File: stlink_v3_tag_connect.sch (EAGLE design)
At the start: 10 parts, among them CON1 STLINK_V3_HAT_SWD/JTAG_MINIMAL, J1 RJ12, U1 SN74LVC2T45DCU

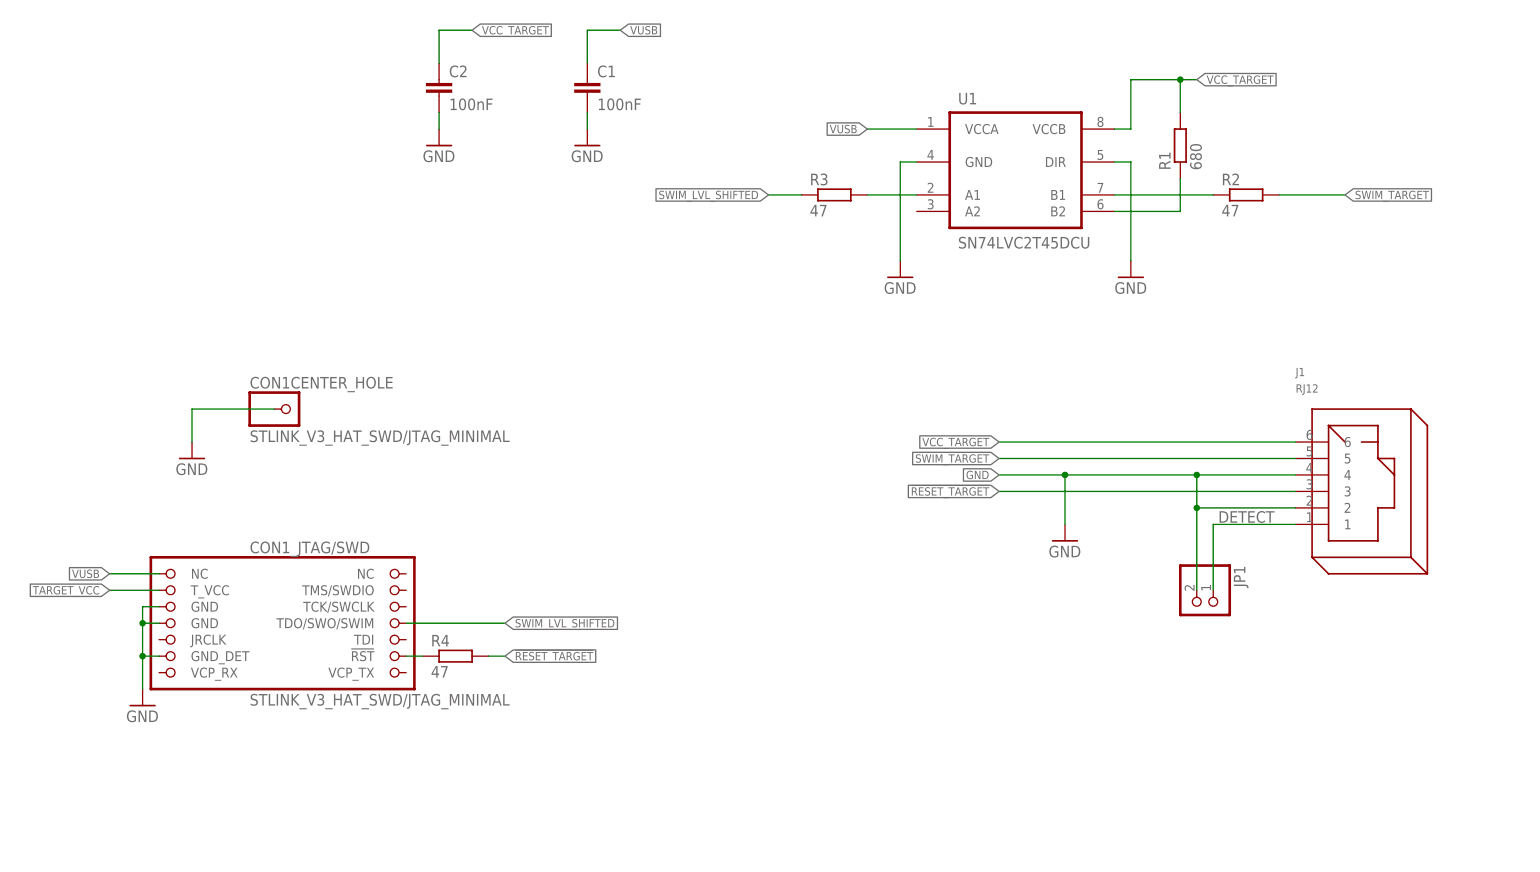
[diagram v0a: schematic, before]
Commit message: Added SWD popoption
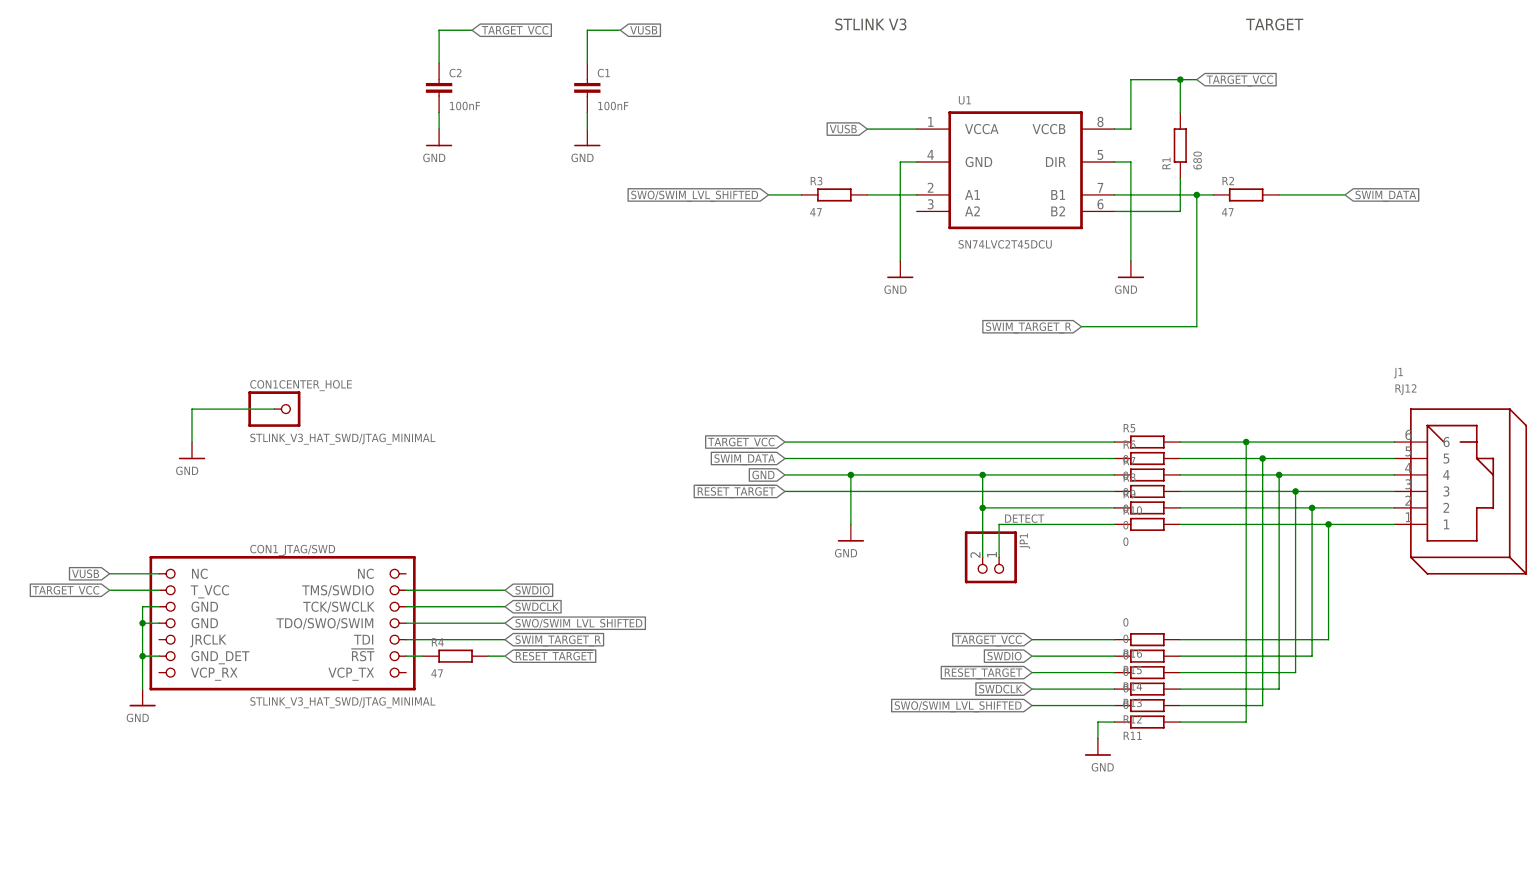
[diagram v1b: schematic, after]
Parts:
- added R10, R11, R12, R13, R14, R15, R16, R5, R6, R7, R8, R9: 0, resistor:R-EU_R0603
- JP1: value (none) -> -
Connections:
- removed net SWIM_LVL_SHIFTED: CON1_JTAG/SWD.TDO/SWO/SWIM, R3.1
- removed net SWIM_TARGET: J1.5, R2.2
- removed net VCC_TARGET: C2.1, J1.6, R1.2, U1.VCCB
- new net N$12: J1.6, R11.2, R5.2
- new net N$3: J1.5, R12.2, R6.2
- new net N$4: J1.4, R13.2, R7.2
- new net N$5: J1.3, R14.2, R8.2
- new net N$6: J1.2, R15.2, R9.2
- new net N$7: J1.1, R10.2, R16.2
- new net SWDCLK: CON1_JTAG/SWD.TCK/SWCLK, R13.1
- new net SWDIO: CON1_JTAG/SWD.TMS/SWDIO, R15.1
- new net SWIM_DATA: R2.2, R6.1
- new net SWO/SWIM_LVL_SHIFTED: CON1_JTAG/SWD.TDO/SWO/SWIM, R12.1, R3.1
- net !RESET_TARGET: now also R14.1, R8.1; no longer J1.3
- net DETECT: now also R10.1; no longer J1.1
- net GND: now also R11.1, R7.1, R9.1; no longer J1.2, J1.4
- net SWIM_TARGET_R: now also CON1_JTAG/SWD.TDI
- net TARGET_VCC: now also C2.1, R1.2, R16.1, R5.1, U1.VCCB
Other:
- note added: "STLINK V3"
- note added: "TARGET"
- moved on the sheet: J1, JP1

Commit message: - Added mgt MCU - Moved RJ12 to the middle - Fixed SWD pinout
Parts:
- removed J1: RJ12, con-rj:RJ12
- added C3: 100nF, rcl:C-EUC0603K
- added C4, C5, C7: 1uF, rcl:C-EUC0603
- added C6: 470pF, rcl:C-EUC0603
- added CON2: TC2030-MCP-SWD, tag-connect:TC2030-MCP-SWD
- added IC1: STM8S003F3, stm8:STM8S003F3
- added LED1, LED2, LED3: Red, SparkFun:LED0603
- added R17: 10K, rcl:R-EU_R0603
- added R18, R19, R20: 1K, rcl:R-EU_R0603
- added SWIM: SWIM_254, swim:SWIM_254
- added U3: MIC5205-3.3YM5-TR, LTC_By_element14_Batch_1:LT1761ES5-3.3TRMPBF
- R11, R16: value 0 -> 10K; device resistor:R-EU_R0603 -> rcl:R-EU_R0603
- R5, R9: value 0 -> 47; device resistor:R-EU_R0603 -> rcl:R-EU_R0603
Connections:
- removed net N$12: J1.6, R11.2, R5.2
- removed net N$6: J1.2, R15.2, R9.2
- removed net N$7: J1.1, R10.2, R16.2
- new net !RESET_TARGET!/SWDCLK: CON2.SWCLK/TCK, R13.2, R8.2
- new net !RST: IC1.!RST, SWIM.!RST
- new net +3V3: C3.1, C5.1, IC1.VDD, R17.1, R19.2, SWIM.VDD, U3.OUT
- new net DETECT/SWO: CON2.SWO/TDO, R10.2, R12.2
- new net DGND: LED1.C, LED2.C, LED3.C
- new net GND/!RESET_TARGET!: CON2.!RESET, R14.2, R7.2
- new net MIC_BYPASS: C6.1, U3.BYP
- new net N$2: CON1_JTAG/SWD.VCP_TX, R5.1
- new net N$38: LED2.A, R18.1
- new net STM8_RX: IC1.PD6/UART1_RX/AIN6, R5.2
- new net STM8_SWIM: IC1.PD1/SWIM, SWIM.DATA
- new net STM8_TX: IC1.PD5/UART1_TX/AIN5, R9.1
- new net SWIM_DATA/SWDIO: CON2.SWDIO/TMS, R15.2, R6.2
- new net TARGET_VCC_DETECT: IC1.PC4/TIM1_CH4/CLK_CCO/AIN2/[!TIM1_CH2!], R11.2, R16.2
- new net VBAT: C4.1, U3.IN, U3.~SHDN
- new net VCAP1: C7.1, IC1.VCAP
- net DETECT: now also IC1.PA3/TIM2_CH3/[SPI_NSS], R17.2
- net GND: now also C3.2, C4.2, C5.2, C6.2, C7.2, CON2.GND, IC1.GND, SWIM.GND, U3.GND; no longer R9.1
- net N$3: now also CON1_JTAG/SWD.VCP_RX, R9.2; no longer J1.5, R12.2, R6.2
- net N$4: now also LED1.A, R19.1; no longer J1.4, R13.2, R7.2
- net N$5: now also LED3.A, R20.1; no longer J1.3, R14.2, R8.2
- net TARGET_VCC: now also CON2.VCC, R18.2; no longer R5.1
- net VUSB: now also R20.2

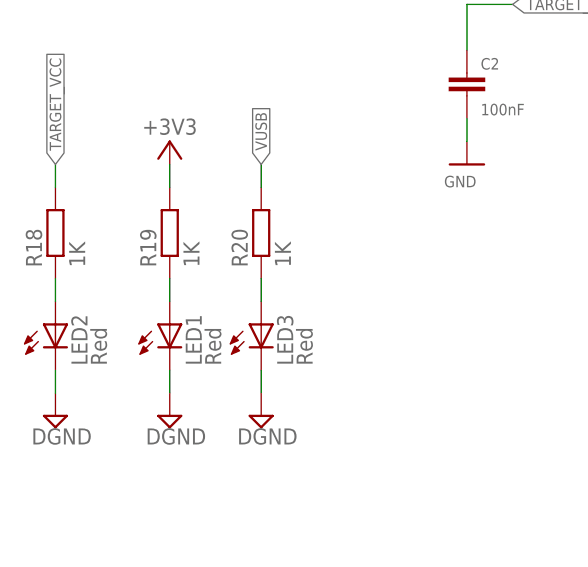
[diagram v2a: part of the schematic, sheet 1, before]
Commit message: Align LEDs
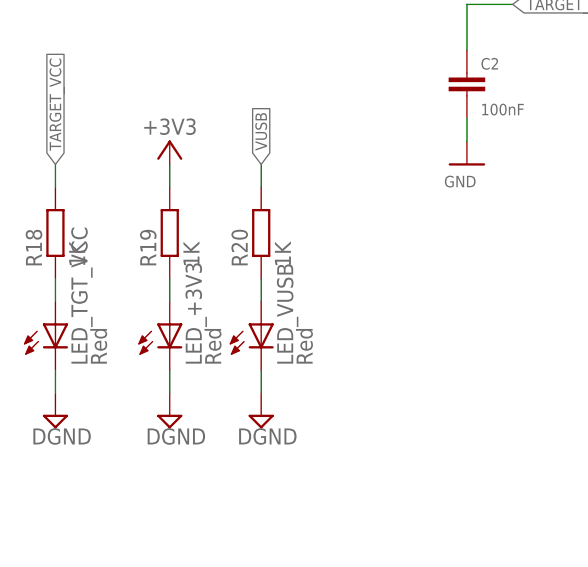
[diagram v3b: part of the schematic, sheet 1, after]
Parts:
- renumbered LED1 to LED_+3V3, LED2 to LED_TGT_VCC, LED3 to LED_VUSB
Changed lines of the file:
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@@
 <attribute name="OC_FARNELL" value="2130354"/>
 </part>
-<part name="LED2" library="SparkFun" deviceset="LED" device="0603" value="Red"/>
+<part name="LED_TGT_VCC" library="SparkFun" deviceset="LED" device="0603" value="Red"/>
 <part name="SUPPLY9" library="supply2" deviceset="DGND" device=""/>
 <part name="R19" library="rcl" deviceset="R-EU_" device="R0603" value="1K">
 <attribute name="OC_FARNELL" value="2130354"/>
 </part>
-<part name="LED1" library="SparkFun" deviceset="LED" device="0603" value="Red"/>
+<part name="LED_+3V3" library="SparkFun" deviceset="LED" device="0603" value="Red"/>
 <part name="SUPPLY1" library="supply2" deviceset="DGND" device=""/>
 <part name="+3V4" library="supply1" deviceset="+3V3" device=""/>
@@
 <attribute name="OC_FARNELL" value="2130354"/>
 </part>
-<part name="LED3" library="SparkFun" deviceset="LED" device="0603" value="Red"/>
+<part name="LED_VUSB" library="SparkFun" deviceset="LED" device="0603" value="Red"/>
 <part name="SUPPLY2" library="supply2" deviceset="DGND" device=""/>
 <part name="FRAME2" library="martonmiklos" deviceset="A4L-LOC" device="" value="PAGE1"/>
@@
 <attribute name="VALUE" x="23.622" y="138.43" size="1.778" layer="96" rot="R90"/>
 </instance>
-<instance part="LED2" gate="G$1" x="20.32" y="132.08" smashed="yes">
+<instance part="LED_TGT_VCC" gate="G$1" x="20.32" y="132.08" smashed="yes">
 <attribute name="NAME" x="23.876" y="127.508" size="1.778" layer="95" rot="R90"/>
 <attribute name="VALUE" x="26.035" y="127.508" size="1.778" layer="96" rot="R90"/>
@@
 <attribute name="VALUE" x="36.322" y="138.43" size="1.778" layer="96" rot="R90"/>
 </instance>
-<instance part="LED1" gate="G$1" x="33.02" y="132.08" smashed="yes">
+<instance part="LED_+3V3" gate="G$1" x="33.02" y="132.08" smashed="yes">
 <attribute name="NAME" x="36.576" y="127.508" size="1.778" layer="95" rot="R90"/>
 <attribute name="VALUE" x="38.735" y="127.508" size="1.778" layer="96" rot="R90"/>
@@
 <attribute name="VALUE" x="46.482" y="138.43" size="1.778" layer="96" rot="R90"/>
 </instance>
-<instance part="LED3" gate="G$1" x="43.18" y="132.08" smashed="yes">
+<instance part="LED_VUSB" gate="G$1" x="43.18" y="132.08" smashed="yes">
 <attribute name="NAME" x="46.736" y="127.508" size="1.778" layer="95" rot="R90"/>
 <attribute name="VALUE" x="48.895" y="127.508" size="1.778" layer="96" rot="R90"/>
@@
 <segment>
 <wire x1="20.32" y1="124.46" x2="20.32" y2="127" width="0.1524" layer="91"/>
-<pinref part="LED2" gate="G$1" pin="C"/>
+<pinref part="LED_TGT_VCC" gate="G$1" pin="C"/>
 <pinref part="SUPPLY9" gate="G$1" pin="DGND"/>
 </segment>
 <segment>
 <wire x1="33.02" y1="124.46" x2="33.02" y2="127" width="0.1524" layer="91"/>
-<pinref part="LED1" gate="G$1" pin="C"/>
+<pinref part="LED_+3V3" gate="G$1" pin="C"/>
 <pinref part="SUPPLY1" gate="G$1" pin="DGND"/>
 </segment>
 <segment>
 <wire x1="43.18" y1="124.46" x2="43.18" y2="127" width="0.1524" layer="91"/>
-<pinref part="LED3" gate="G$1" pin="C"/>
+<pinref part="LED_VUSB" gate="G$1" pin="C"/>
 <pinref part="SUPPLY2" gate="G$1" pin="DGND"/>
 </segment>
@@
 <wire x1="20.32" y1="134.62" x2="20.32" y2="137.16" width="0.1524" layer="91"/>
 <pinref part="R18" gate="G$1" pin="1"/>
-<pinref part="LED2" gate="G$1" pin="A"/>
+<pinref part="LED_TGT_VCC" gate="G$1" pin="A"/>
 </segment>
 </net>
@@
 <wire x1="33.02" y1="134.62" x2="33.02" y2="137.16" width="0.1524" layer="91"/>
 <pinref part="R19" gate="G$1" pin="1"/>
-<pinref part="LED1" gate="G$1" pin="A"/>
+<pinref part="LED_+3V3" gate="G$1" pin="A"/>
 </segment>
 </net>
@@
 <wire x1="43.18" y1="134.62" x2="43.18" y2="137.16" width="0.1524" layer="91"/>
 <pinref part="R20" gate="G$1" pin="1"/>
-<pinref part="LED3" gate="G$1" pin="A"/>
-</segment>
-</net>
+<pinref part="LED_VUSB" gate="G$1" pin="A"/>
+</segment>
+</net>
